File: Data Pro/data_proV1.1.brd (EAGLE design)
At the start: 98.7 x 80 mm, 57 parts, among them IC1 4049N, IC2 MCP3008, IC3 OP11S, IC6 AT24CP, J1 RASPBERRYPI-40-PIN-GPIO, U1 DS18B20, U2 TPS61200, X1 32.768khz

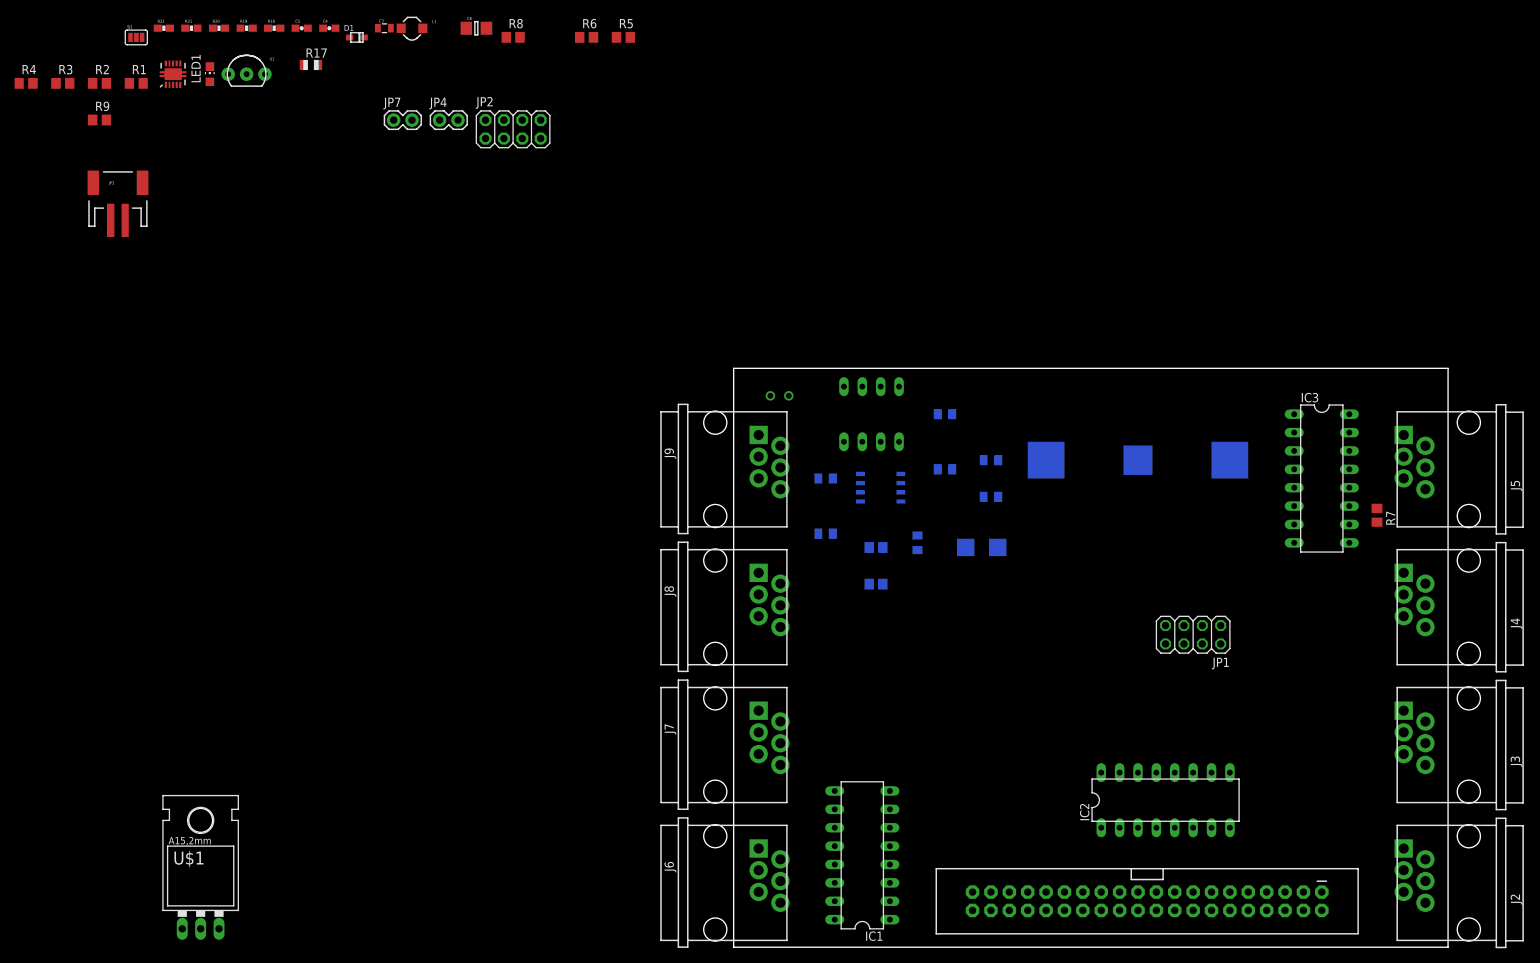
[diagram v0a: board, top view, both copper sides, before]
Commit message: Data pro update v1.2
The schematic is complete, working on the board.
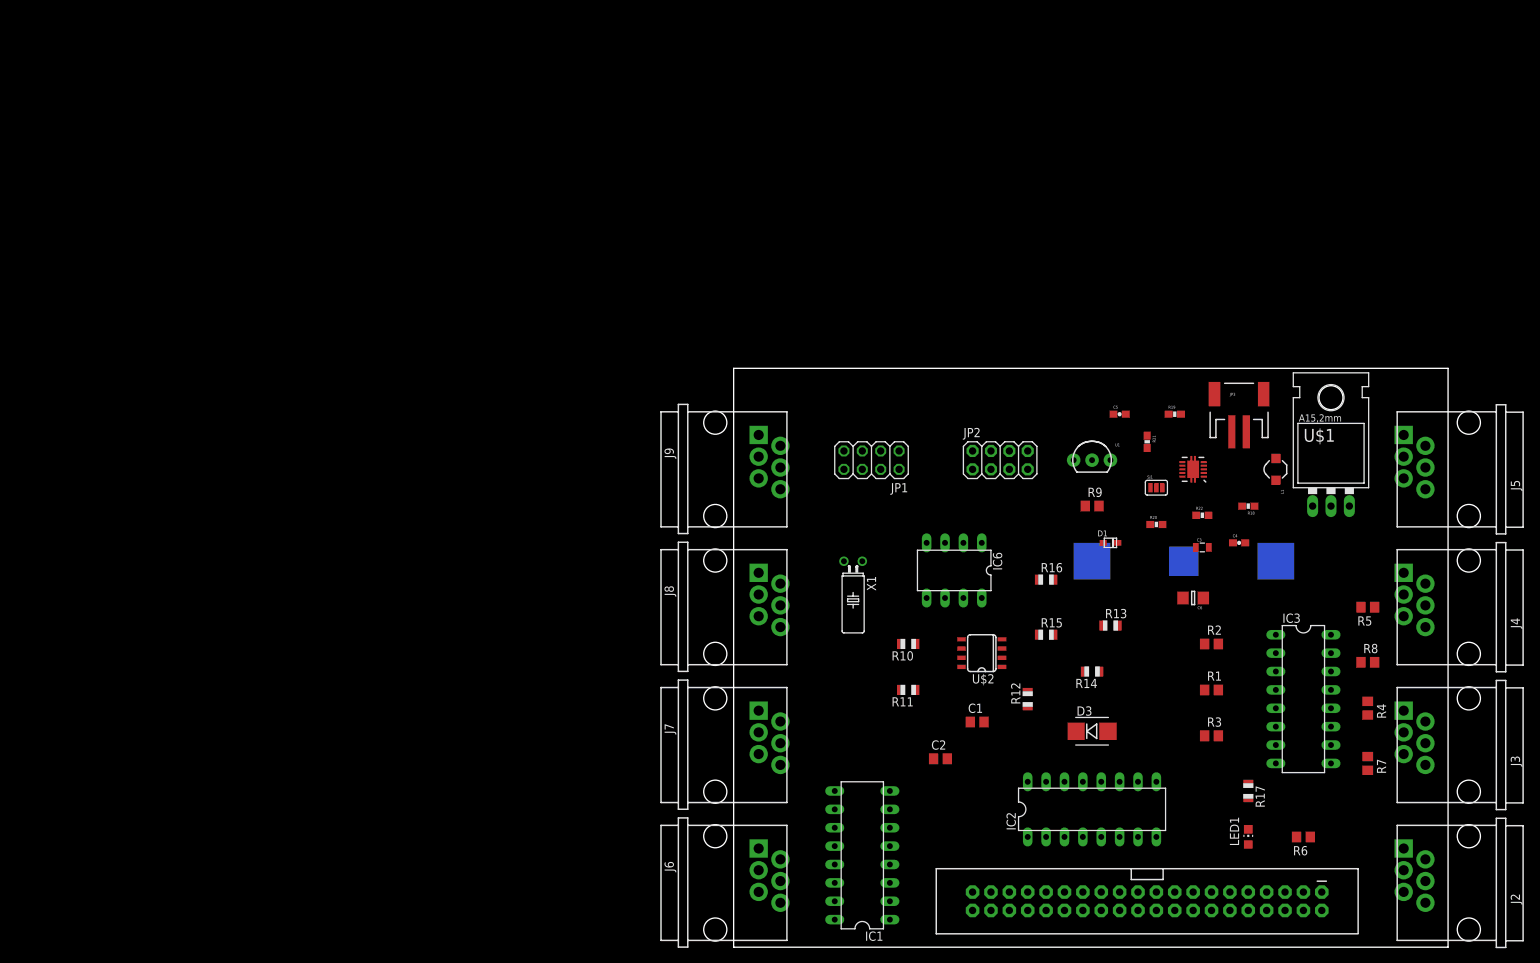
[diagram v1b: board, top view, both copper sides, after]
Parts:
- removed JP4: VOUT, SparkFun:1X02
- removed JP7: VIN, SparkFun:1X02
- R1, R2, R3, R4, R5, R6, R7, R8: value (none) -> 1k
- moved R4 204.5 mm to (87.6, 33.0), turned to 270 degrees
- moved R3 182.6 mm to (66.0, 29.2)
- moved LED1 178.1 mm to (71.1, 15.2)
- moved R2 172.1 mm to (66.0, 41.9)
- moved R1 170.6 mm to (66.0, 35.6)
- moved U$1 166.8 mm to (82.5, 64.8)
- moved R17 163.8 mm to (71.1, 21.6), turned to 270 degrees
- moved R22 158.5 mm to (64.8, 59.7)
- moved JP3 157.7 mm to (69.8, 74.9)
- moved SJ1 154.1 mm to (58.4, 63.5)
- moved U2 151.2 mm to (63.5, 66.0), turned to 90 degrees
- moved R18 149.9 mm to (71.1, 61.0), turned to 180 degrees
- moved R6 148.4 mm to (78.7, 15.2), turned to 180 degrees
- moved R9 147.2 mm to (49.5, 61.0)
- moved R20 146.6 mm to (58.4, 58.4)
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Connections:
- new net S$1: R22.2
- new net S$3: JP3.1
- new net S$5: C4.2, R18.1
- new net S$7: JP3.2
- net GND: no longer JP1.1, JP3.1, JP4.1, JP7.1, U2.11, U2.12, U2.13, U2.14, U2.15, U2.4, U2.9
- net N$13: no longer U2.1
- net UVLO: no longer C4.2, R18.1
- net VCC: no longer JP4.2, R22.2, U2.2
- net VIN: no longer JP3.2, JP7.2, L1.P$2, U2.8
